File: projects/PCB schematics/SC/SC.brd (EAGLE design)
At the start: 132.1 x 81 mm, 75 parts, among them X1 5566-10, X2 5566-2, X4 5566-12

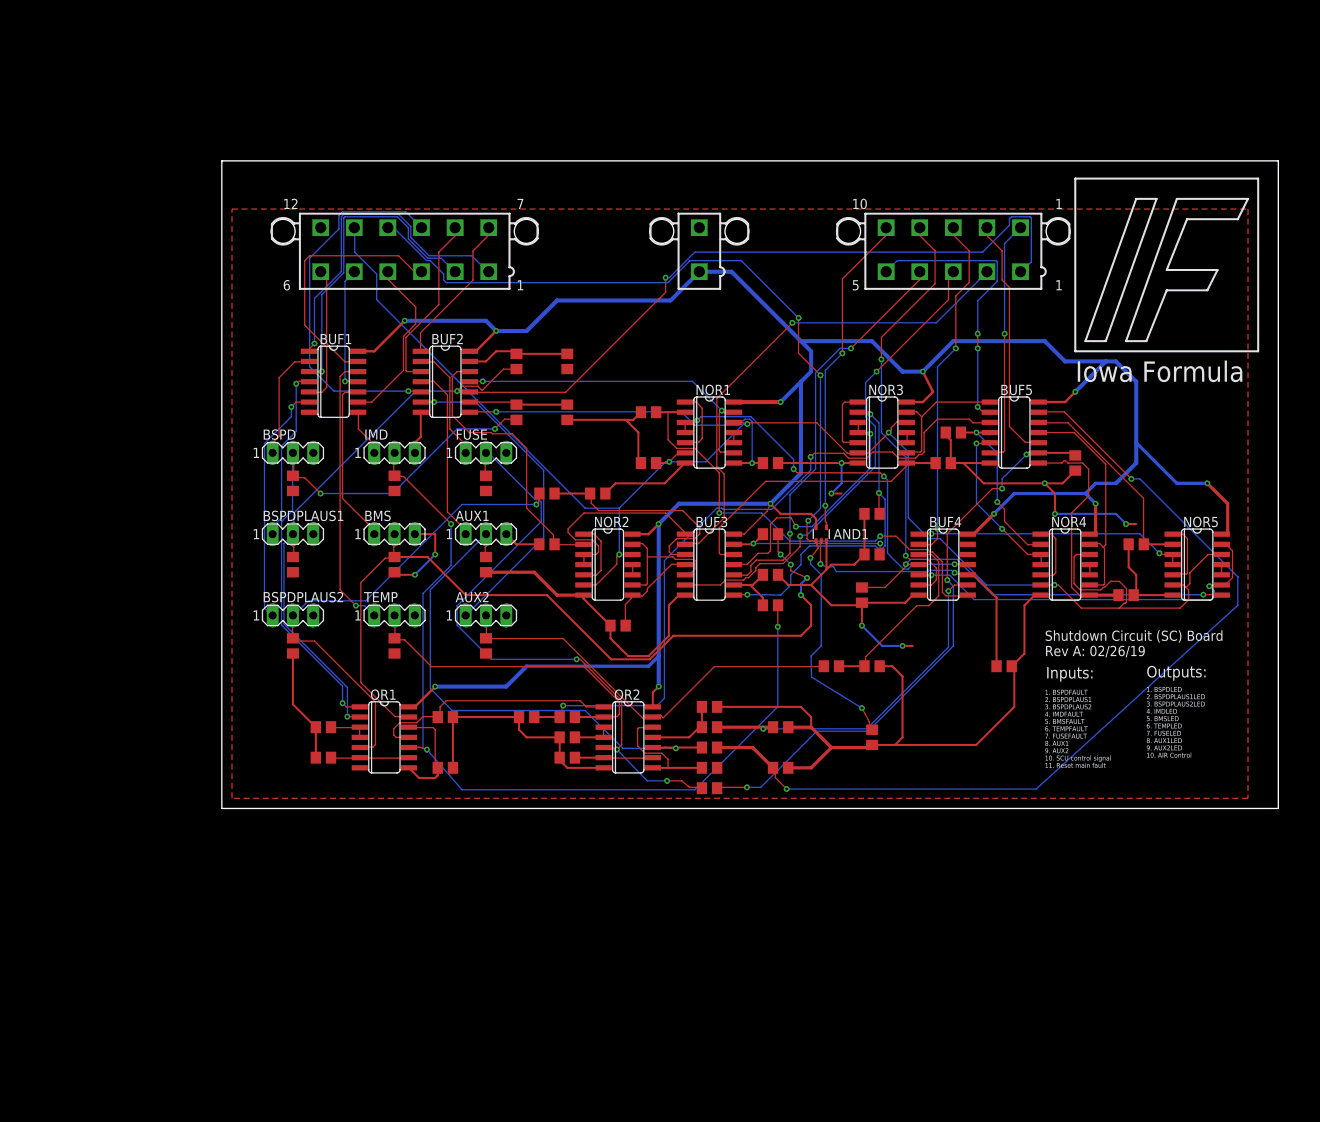
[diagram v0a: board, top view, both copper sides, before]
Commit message: TSMPC - Initial draft (WIP).
Non-working commit of TSMPC.
Done simply to show possible board layout.
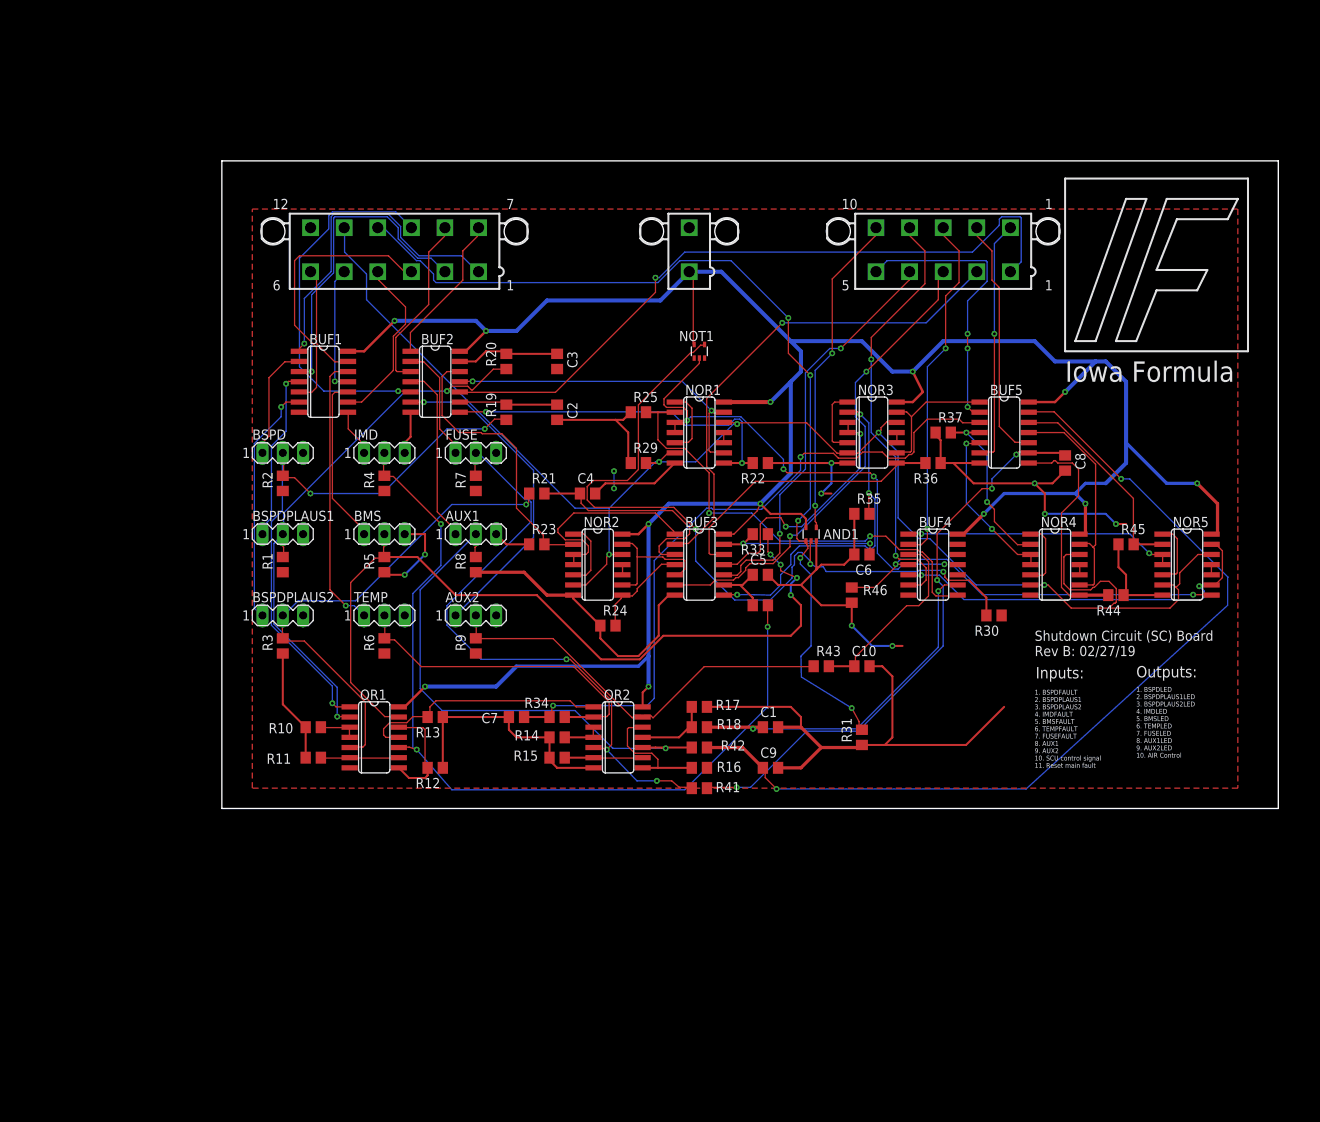
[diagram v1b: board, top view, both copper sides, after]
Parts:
- added NOT1: 74AUC1G14DCK, 74xx-little-us:SC70-5
- moved R30 6.48 mm to (96.5, 24.1)
- moved AND1 1.27 mm to (73.7, 34.3)
- moved C8 1.27 mm to (105.4, 43.2)
- moved R46 1.27 mm to (78.7, 26.7)
- moved AUX1 1.27 mm to (31.8, 34.3)
- moved AUX2 1.27 mm to (31.8, 24.1)
- moved BUF3 1.27 mm to (59.7, 30.5)
- moved C2 1.27 mm to (41.9, 49.5)
- moved C3 1.27 mm to (41.9, 55.9)
- moved C4 1.27 mm to (45.7, 39.4)
- moved C7 1.27 mm to (36.8, 11.4)
- moved FUSE 1.27 mm to (31.8, 44.5)
- moved NOR1 1.27 mm to (59.7, 47.0)
- moved R14 1.27 mm to (41.9, 8.89)
- moved R15 1.27 mm to (41.9, 6.35)
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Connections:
- net GND: now also NOT1.3
- net N$8: now also NOT1.4; no longer BUF4.10
- net Q: now also NOT1.2; no longer BUF4.11
- net VCC: now also NOT1.5
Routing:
- net N$8: track 35.5 -> 98.0 mm, vias 2 -> 3
- net GND: track 318.0 -> 298.3 mm, vias 9 -> 11
- net Q: track 51.2 -> 61.6 mm
- net VCC: track 315.3 -> 324.7 mm
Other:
- board text added: "Shutdown Circuit (SC) Board Rev B: 02/27/19"
- board text removed: "Shutdown Circuit (SC) Board Rev A: 02/26/19"

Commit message: SC - Rev C; SC70 -> SOT23.
For single logic gate components, SC70 was initially chosen.
These packages proved too small to hand-solder.

All SC70 packages have been refactored to SOT23.

SparkFun DRC's added in for additional manufacturability.
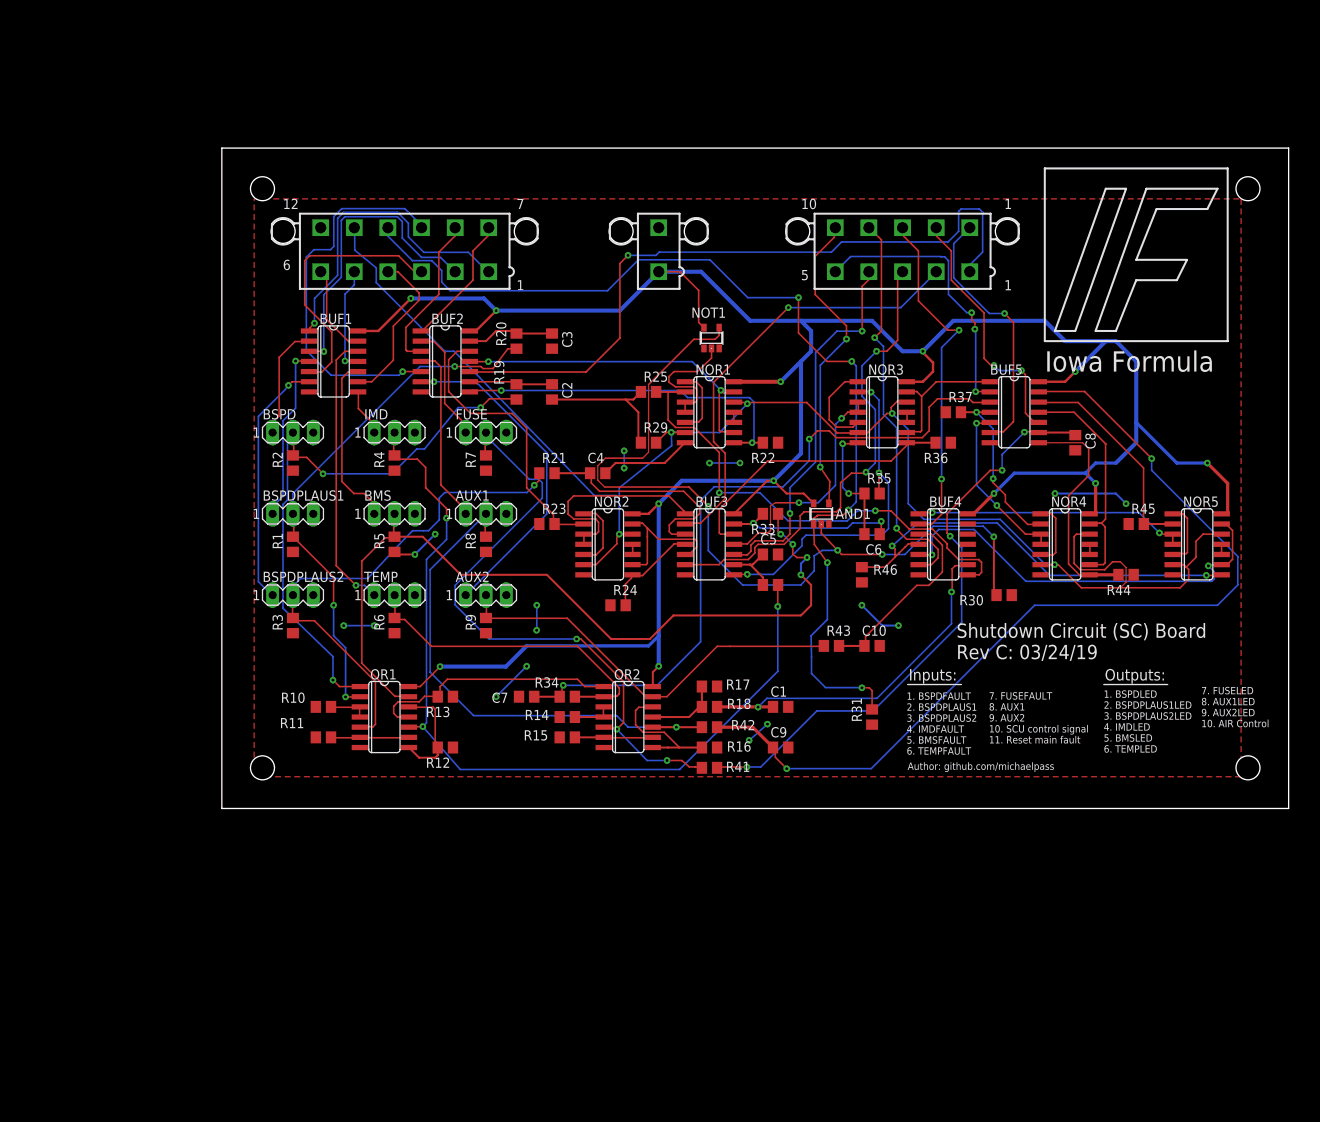
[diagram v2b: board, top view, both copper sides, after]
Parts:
- AND1: value 74LVC1G08DCK -> 74LVC1G08DBV; device 74xx-little-us:SC70-5 -> 74xx-little-us:SOT23-5
- NOT1: value 74AUC1G14DCK -> 74AUC1G14DBV; device 74xx-little-us:SC70-5 -> 74xx-little-us:SOT23-5
- moved X1 5.08 mm to (85.1, 69.8)
- moved X2 3.81 mm to (54.6, 69.8)
- moved R30 2.84 mm to (97.8, 26.7)
- moved AND1 2.84 mm to (74.9, 36.8)
- moved AUX2 2.84 mm to (33.0, 26.7)
- moved BUF3 2.84 mm to (61.0, 33.0)
- moved C8 2.84 mm to (106.7, 45.7)
- moved R46 2.84 mm to (80.0, 29.2)
- moved R8 2.84 mm to (33.0, 33.0)
- moved BSPDPLAUS2 2.84 mm to (8.89, 26.7)
- moved R1 2.84 mm to (8.89, 33.0)
- moved C7 2.84 mm to (38.1, 14.0)
- moved R15 2.84 mm to (43.2, 8.89)
- moved R17 2.84 mm to (61.0, 15.2)
- moved R34 2.84 mm to (43.2, 14.0)
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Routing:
- net GND: track 298.3 -> 87.7 mm, vias 11 -> 20
- net Q: track 61.6 -> 16.3 mm, vias 4 -> 0
- net SCU_CONTROL: track 119.0 -> 127.6 mm
- net BSPDPLAUS1_LED: track 62.0 -> 55.1 mm
- net N$8: track 98.0 -> 104.4 mm, vias 3 -> 4
- net SET_AUX2: track 50.1 -> 54.9 mm
- net Q_AUX2: track 48.3 -> 53.0 mm
- net AUX2_LED: track 54.3 -> 49.9 mm
- net IMDFAULT_LED: track 51.3 -> 47.2 mm
- net BSPDPLAUS1_O: track 69.5 -> 66.0 mm, vias 2 -> 3
- net TEMPFAULT: track 14.2 -> 11.4 mm
- net SET_MAINFAULT: track 58.4 -> 61.1 mm
- net ~Q_IMDFAULT: track 8.59 -> 11.3 mm
- net AUX1: track 22.3 -> 19.8 mm
- net BMSFAULT: track 15.8 -> 13.3 mm
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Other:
- board size 132.1 x 81 mm -> 133.3 x 82.5 mm
- board text added: "1. BSPDFAULT 2. BSPDPLAUS1 3. BSPDPLAUS2 4. IMDFAULT 5. BMSFAULT 6. TEMPFAULT"
- board text added: "1. BSPDLED 2. BSPDPLAUS1LED 3. BSPDPLAUS2LED 4. IMDLED 5. BMSLED 6. TEMPLED"
- board text added: "7. FUSEFAULT 8. AUX1 9. AUX2 10. SCU control signal 11. Reset main fault"
- board text added: "7. FUSELED 8. AUX1LED 9. AUX2LED 10. AIR Control"
- board text added: "Author: github.com/michaelpass"
- board text added: "POWER"
- board text added: "Shutdown Circuit (SC) Board Rev C: 03/24/19"
- board text removed: "1. BSPDFAULT 2. BSPDPLAUS1 3. BSPDPLAUS2 4. IMDFAULT 5. BMSFAULT 6. TEMPFAULT 7. FUSEFAULT 8. AUX1 9. AUX2 10. SCU control signal 11. Reset main fault"
- board text removed: "1. BSPDLED 2. BSPDPLAUS1LED 3. BSPDPLAUS2LED 4. IMDLED 5. BMSLED 6. TEMPLED 7. FUSELED 8. AUX1LED 9. AUX2LED 10. AIR Control"
- board text removed: "Shutdown Circuit (SC) Board Rev B: 02/27/19"

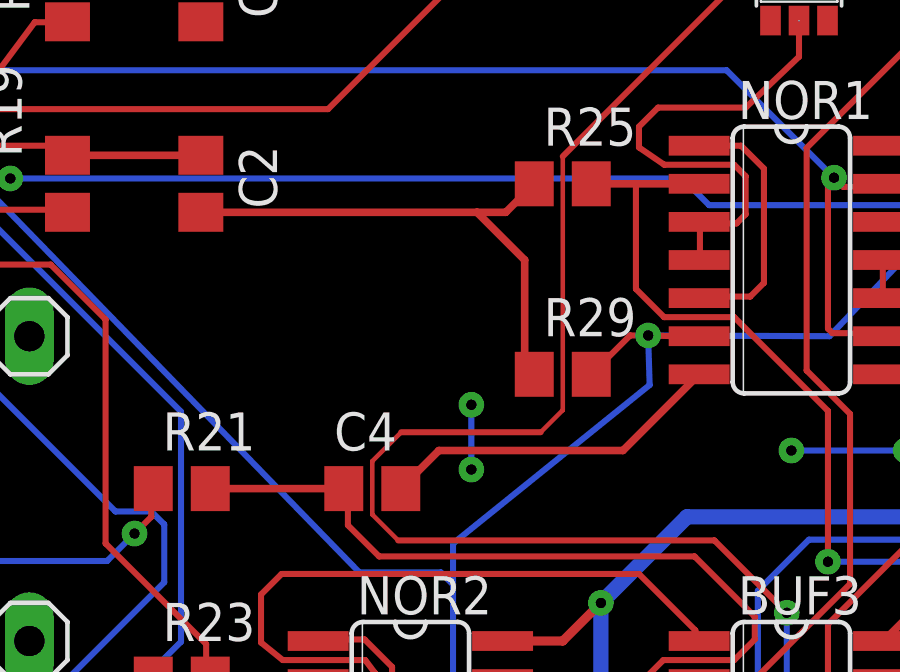
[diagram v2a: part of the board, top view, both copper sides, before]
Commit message: BSPD - Schematic revision/component revision.
During ESF, schematics chosen used European part libraries.
These were updated to US symbols, with appropriate final parts sourced
to allow builds of both SOP8 and DIL-8 packages.
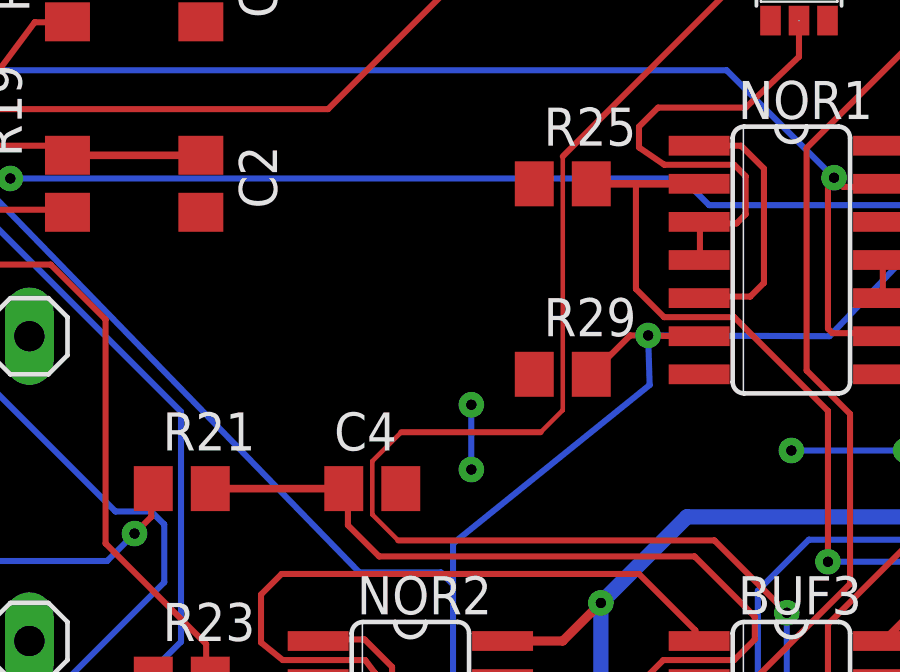
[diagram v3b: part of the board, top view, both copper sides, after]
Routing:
- net GND: track 87.7 -> 59.0 mm
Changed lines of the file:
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@@
 <contactref element="BUF2" pad="7"/>
 <contactref element="NOR1" pad="7"/>
-<wire x1="47.94" y1="41.91" x2="49.21" y2="43.18" width="0.254" layer="1"/>
-<wire x1="49.21" y1="43.18" x2="55.3466" y2="43.18" width="0.254" layer="1"/>
-<wire x1="57.8866" y1="45.72" x2="55.3466" y2="43.18" width="0.254" layer="1"/>
-<wire x1="41.275" y1="51.12" x2="50.48" y2="51.12" width="0.254" layer="1"/>
-<wire x1="50.48" y1="51.12" x2="51.44" y2="51.12" width="0.254" layer="1"/>
-<wire x1="51.44" y1="51.12" x2="52.39" y2="52.07" width="0.254" layer="1"/>
 <wire x1="42.23" y1="8.57" x2="42.23" y2="8.89" width="0.254" layer="1"/>
 <wire x1="80.33" y1="34.29" x2="80.33" y2="39.37" width="0.254" layer="1"/>
 <wire x1="52.39" y1="45.72" x2="52.07" y2="46.04" width="0.254" layer="1"/>
-<wire x1="52.07" y1="46.04" x2="52.07" y2="49.53" width="0.254" layer="1"/>
-<wire x1="52.07" y1="49.53" x2="50.48" y2="51.12" width="0.254" layer="1"/>
 <via x="77.597" y="45.593" extent="1-16" drill="0.35"/>
 <via x="104.14" y="39.37" extent="1-16" drill="0.35"/>

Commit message: TEMP - Initial board placement.
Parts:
- moved R32 96.8 mm to (-24.1, 55.9)
- moved X2 63.2 mm to (71.1, 8.89), turned to 180 degrees
- moved R44 46.7 mm to (81.3, 63.5)
- moved R45 45.8 mm to (81.3, 67.3)
- moved C10 44.9 mm to (48.3, 50.8)
- moved R43 44.2 mm to (48.3, 54.6)
- moved C6 44.1 mm to (48.3, 63.5)
- moved AND1 43.4 mm to (48.3, 71.1)
- moved R46 43.1 mm to (48.3, 58.4), turned to 180 degrees
- moved R35 41.4 mm to (41.9, 52.1)
- moved R31 39.4 mm to (81.3, 50.8), turned to 180 degrees
- moved NOR5 38.8 mm to (88.9, 53.3)
- moved C5 38.6 mm to (41.9, 59.7)
- moved R33 38.6 mm to (41.9, 64.8)
- moved NOR4 36.9 mm to (88.9, 66.0)
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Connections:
- net AUX1: now also R42.1; no longer BUF2.3
- net AUX1_LED: now also BUF2.3
- net AUX1_O: no longer R42.1
- net AUX2: now also R43.1; no longer BUF2.5
- net AUX2_LED: now also BUF2.5
- net AUX2_O: no longer R43.1
- net BMSFAULT: now also R33.1; no longer BUF1.11
- net BMSFAULT_LED: now also BUF1.11
- net BMSFAULT_O: no longer R33.1
- net BSPDFAULT: now also R19.1; no longer BUF1.1
- net BSPDFAULT_LED: now also BUF1.1
- net BSPDFAULT_O: no longer R19.1
- net BSPDPLAUS1: now also R20.1; no longer BUF1.3
- net BSPDPLAUS1_LED: now also BUF1.3
- net BSPDPLAUS1_O: no longer R20.1
- net BSPDPLAUS2: now also R21.1; no longer BUF1.5
- net BSPDPLAUS2_LED: now also BUF1.5
- net BSPDPLAUS2_O: no longer R21.1
- net FUSEFAULT: now also R41.1; no longer BUF2.1
- net FUSEFAULT_LED: now also BUF2.1
- net FUSEFAULT_O: no longer R41.1
- net IMDFAULT: now also R32.1; no longer BUF1.9
- net IMDFAULT_LED: now also BUF1.9
- net IMDFAULT_O: no longer R32.1
- net TEMPFAULT: now also R34.1; no longer BUF1.13
- net TEMPFAULT_LED: now also BUF1.13
- net TEMPFAULT_O: no longer R34.1
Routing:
- net VCC: track 323.5 -> 0.00 mm, vias 12 -> 0
- net RESET_MAINFAULT: track 195.2 -> 0.00 mm, vias 5 -> 0
- net SCU_CONTROL: track 127.6 -> 0.00 mm, vias 5 -> 0
- net N$16: track 115.2 -> 0.00 mm, vias 2 -> 0
- net IMDFAULT_O: track 106.7 -> 0.00 mm, vias 3 -> 0
- net N$8: track 104.4 -> 0.00 mm, vias 4 -> 0
- net BMSFAULT_O: track 102.6 -> 0.00 mm, vias 4 -> 0
- net BSPDFAULT_LED: track 87.8 -> 0.00 mm, vias 1 -> 0
- net N$10: track 87.5 -> 0.00 mm, vias 2 -> 0
- net FUSEFAULT_O: track 78.3 -> 0.00 mm, vias 3 -> 0
- net N$15: track 74.1 -> 0.00 mm, vias 4 -> 0
- net BSPDFAULT_O: track 73.9 -> 0.00 mm, vias 3 -> 0
- net BSPDPLAUS1_O: track 66.0 -> 0.00 mm, vias 3 -> 0
- net AUX1_O: track 65.8 -> 0.00 mm, vias 1 -> 0
- net BSPDPLAUS2_O: track 64.0 -> 0.00 mm, vias 1 -> 0
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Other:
- board size 133.3 x 82.5 mm -> 99.1 x 99.1 mm
- board text added: "Shutdown Circuit (SC) Board Rev D: 04/28/19"
- board text removed: "1"
- board text removed: "10"
- board text removed: "12"
- board text removed: "5"
- board text removed: "6"
- board text removed: "7"
- board text removed: "Iowa Formula"
- board text removed: "Shutdown Circuit (SC) Board Rev C: 03/24/19"
